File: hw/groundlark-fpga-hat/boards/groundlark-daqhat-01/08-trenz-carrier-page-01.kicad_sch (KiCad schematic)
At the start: 6 parts, among them J83 1715721

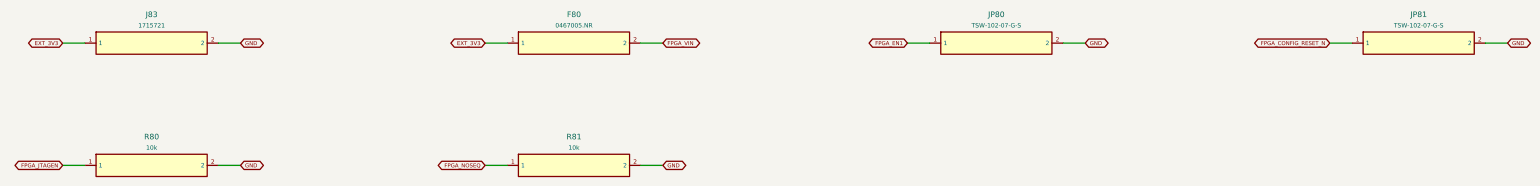
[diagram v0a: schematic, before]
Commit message: Add TI Pi power supervision and expand DAQHAT enclosure
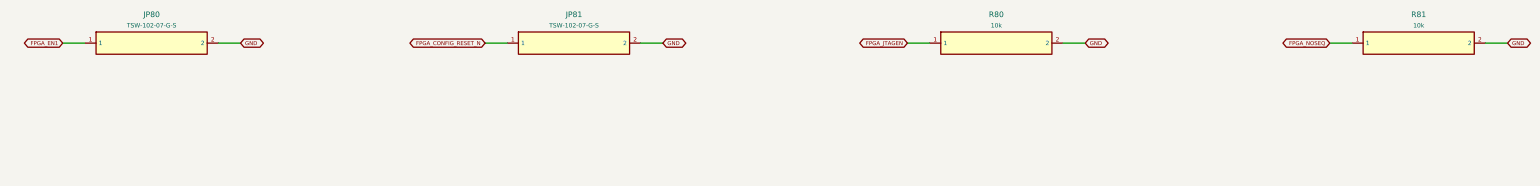
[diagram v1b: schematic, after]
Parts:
- removed F80: 0467005.NR, Groundlark:TZ_TZ_FUSE, symbol Groundlark:Part_F80
- removed J83: 1715721, Groundlark:TZ_TZ_POWER, symbol Groundlark:Part_J83
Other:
- moved on the sheet: JP80, JP81, R80, R81
